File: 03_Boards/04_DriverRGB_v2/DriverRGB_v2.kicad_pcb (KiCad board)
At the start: 2 copper layers, 30 x 45 mm, 22 parts, among them J1 PJ-102A, J2 S4B-ZR-SM4A, J3 AMPHENOL_20021121-00006C1LF, Q1 DPAK3-CASE-369AS, Q2 DPAK3-CASE-369AS, Q3 DPAK3-CASE-369AS, U1 MODULE_ESP-12S, U3 AMS1117CD-3.3

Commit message: Docimentation
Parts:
- moved J1 1.68 mm to (142.3, 85.0)
- moved C3 1.31 mm to (140.8, 81.9)
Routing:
- net GND: track 55.1 -> 56.8 mm
- net PWR_IN: track 65.7 -> 66.8 mm
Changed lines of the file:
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@@
     (pad_to_mask_clearance 0)
     (pcbplotparams
-      (layerselection 0x003ffff_ffffffff)
+      (layerselection 0x003f0ff_ffffffff)
       (plot_on_all_layers_selection 0x0000000_00000000)
       (disableapertmacros false)
@@
       (dashed_line_gap_ratio 3.000000)
       (svgprecision 4)
-      (plotframeref false)
+      (plotframeref true)
       (viasonmask false)
       (mode 1)
@@
   )
   (footprint "01_Footprints:PJ-102AH" (layer "F.Cu")
-    (at 142.367 86.6394)
+    (at 142.3162 84.963)
     (descr "PJ-102AH")
     (tags "Connector")
@@
     (property "ki_keywords" "CP-102A-ND")
     (attr through_hole)
-    (fp_text reference "J1" (at -1.905 -8.89) (layer "F.SilkS")
+    (fp_text reference "J1" (at -1.9304 -7.8994) (layer "F.SilkS")
         (effects (font (size 1.27 1.27) (thickness 0.254) bold))
     )
@@
         (effects (font (size 1.27 1.27) (thickness 0.254)))
     )
-    (fp_line (start 0 -10.7) (end 0 -3.5)
+    (fp_line (start 0 -9.144) (end 0 -3.5)
       (stroke (width 0.2) (type solid)) (layer "F.SilkS"))
-    (fp_line (start 9 -10.7) (end 0 -10.7)
+    (fp_line (start 9 -9.144) (end 0 -9.144)
       (stroke (width 0.2) (type solid)) (layer "F.SilkS"))
-    (fp_line (start 9 3.7) (end 9 -10.7)
+    (fp_line (start 9 3.7) (end 9 -9.144)
       (stroke (width 0.2) (type solid)) (layer "F.SilkS"))
     (fp_circle (center 4.261 5.051) (end 4.261 5.16985)
@@
   )
   (footprint "Capacitor_SMD:C_0603_1608Metric" (layer "B.Cu")
-    (at 140.843 83.1974 90)
+    (at 140.843 81.8896 90)
     (descr "Capacitor SMD 0603 (1608 Metric), square (rectangular) end terminal, IPC_7351 nominal, (Body size source: IPC-SM-782 page 76, https://www.pcb-3d.com/wordpress/wp-content/uploads/ipc-sm-782a_amendment_1_and_2.pdf), generated with kicad-footprint-generator")
     (tags "capacitor")
@@
     (property "ki_keywords" "cap capacitor")
     (attr smd)
-    (fp_text reference "C3" (at -0.013 1.778 180) (layer "B.SilkS")
+    (fp_text reference "C3" (at 1.143 -1.8034 180) (layer "B.SilkS")
         (effects (font (size 1 1) (thickness 0.2) bold) (justify mirror))
     )
@@
   (segment (start 142.748 116.4354) (end 143.764 115.4194) (width 0.3) (layer "B.Cu") (net 1))
   (segment (start 147.3454 101.6762) (end 148.336 102.6668) (width 0.7) (layer "F.Cu") (net 2))
-  (segment (start 140.1378 100.36545) (end 140.1378 88.4686) (width 0.7) (layer "F.Cu") (net 2))
   (segment (start 146.3548 102.6414) (end 147.326 101.6702) (width 0.7) (layer "F.Cu") (net 2))
+  (segment (start 140.1378 86.7414) (end 141.9162 84.963) (width 0.7) (layer "F.Cu") (net 2))
   (segment (start 141.1478 102.6414) (end 146.3548 102.6414) (width 0.7) (layer "F.Cu") (net 2))
   (segment (start 140.1378 100.36545) (end 140.1378 101.6314) (width 0.7) (layer "F.Cu") (net 2))
@@
   (segment (start 147.3454 100.3808) (end 147.3454 101.6762) (width 0.7) (layer "F.Cu") (net 2))
   (segment (start 147.326 101.6702) (end 147.326 100.3816) (width 0.7) (layer "F.Cu") (net 2))
-  (segment (start 140.1378 88.4686) (end 141.967 86.6394) (width 0.7) (layer "F.Cu") (net 2))
+  (segment (start 140.1378 100.36545) (end 140.1378 86.7414) (width 0.7) (layer "F.Cu") (net 2))
   (segment (start 140.1378 101.6314) (end 141.1478 102.6414) (width 0.7) (layer "F.Cu") (net 2))
   (segment (start 153.6192 102.6668) (end 154.6218 101.6642) (width 0.7) (layer "F.Cu") (net 2))
@@
   (segment (start 154.051 118.1354) (end 151.498 118.1354) (width 0.3) (layer "B.Cu") (net 3))
   (segment (start 138.557 80.9244) (end 138.557 83.0304) (width 0.3) (layer "B.Cu") (net 4))
+  (segment (start 138.9228 82.6646) (end 138.557 83.0304) (width 0.3) (layer "B.Cu") (net 4))
   (segment (start 153.914 82.9244) (end 153.914 82.4384) (width 0.3) (layer "B.Cu") (net 4))
-  (segment (start 138.885 83.0304) (end 138.557 83.0304) (width 0.3) (layer "B.Cu") (net 4))
-  (segment (start 140.843 83.9724) (end 139.827 83.9724) (width 0.3) (layer "B.Cu") (net 4))
+  (segment (start 140.843 82.6646) (end 138.9228 82.6646) (width 0.3) (layer "B.Cu") (net 4))
   (segment (start 153.914 82.4384) (end 151.257 79.7814) (width 0.3) (layer "B.Cu") (net 4))
-  (segment (start 139.827 83.9724) (end 138.885 83.0304) (width 0.3) (layer "B.Cu") (net 4))
   (segment (start 151.257 79.7814) (end 139.7 79.7814) (width 0.3) (layer "B.Cu") (net 4))
   (segment (start 139.7 79.7814) (end 138.557 80.9244) (width 0.3) (layer "B.Cu") (net 4))
@@
   (segment (start 154.5696 95.032) (end 151.638 92.1004) (width 0.3) (layer "B.Cu") (net 5))
   (segment (start 154.5696 96.5446) (end 154.5696 95.1776) (width 0.3) (layer "B.Cu") (net 5))
+  (segment (start 144.7398 116.3128) (end 145.3686 116.9416) (width 0.7) (layer "F.Cu") (net 6))
+  (segment (start 152.7076 87.963) (end 146.6162 87.963) (width 0.7) (layer "F.Cu") (net 6))
+  (segment (start 154.686 116.9416) (end 160.9598 110.6678) (width 0.7) (layer "F.Cu") (net 6))
+  (segment (start 144.7398 115.0112) (end 144.7398 116.3128) (width 0.7) (layer "F.Cu") (net 6))
+  (segment (start 160.9598 96.2152) (end 152.7076 87.963) (width 0.7) (layer "F.Cu") (net 6))
   (segment (start 160.9598 110.6678) (end 160.9598 96.2152) (width 0.7) (layer "F.Cu") (net 6))
-  (segment (start 144.7398 116.3128) (end 145.3686 116.9416) (width 0.7) (layer "F.Cu") (net 6))
-  (segment (start 144.7398 115.0112) (end 144.7398 116.3128) (width 0.7) (layer "F.Cu") (net 6))
-  (segment (start 160.9598 96.2152) (end 154.384 89.6394) (width 0.7) (layer "F.Cu") (net 6))
   (segment (start 145.3686 116.9416) (end 154.686 116.9416) (width 0.7) (layer "F.Cu") (net 6))
-  (segment (start 154.686 116.9416) (end 160.9598 110.6678) (width 0.7) (layer "F.Cu") (net 6))
-  (segment (start 146.842 89.4644) (end 146.667 89.6394) (width 0.7) (layer "F.Cu") (net 6))
-  (segment (start 154.384 89.6394) (end 146.667 89.6394) (width 0.7) (layer "F.Cu") (net 6))
-  (segment (start 157.373 89.4644) (end 146.842 89.4644) (width 0.3) (layer "B.Cu") (net 6))
-  (segment (start 159.014 91.1054) (end 157.373 89.4644) (width 0.3) (layer "B.Cu") (net 6))
+  (segment (start 155.8716 87.963) (end 146.6162 87.963) (width 0.3) (layer "B.Cu") (net 6))
   (segment (start 159.014 91.6244) (end 159.014 91.1054) (width 0.3) (layer "B.Cu") (net 6))
-  (segment (start 146.842 89.4644) (end 146.667 89.6394) (width 0.3) (layer "B.Cu") (net 6))
+  (segment (start 159.014 91.1054) (end 155.8716 87.963) (width 0.3) (layer "B.Cu") (net 6))
   (segment (start 149.2398 114.4428) (end 156.9018 106.7808) (width 0.7) (layer "F.Cu") (net 7))
   (segment (start 149.2398 115.0112) (end 149.2398 114.4428) (width 0.7) (layer "F.Cu") (net 7))

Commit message: PCB
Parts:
- added R8: 10kOhm, Resistor_SMD:R_0603_1608Metric, B.Cu at (151.2, 117.2)
- C1, C2: value 100nF -> 1nF
- J3: value AMPHENOL_20021121-00006C1LF -> 20021121-00006C1LF
- Q1, Q2, Q3: value DPAK3-CASE-369AS -> FDD8880
- S1: value Enable -> Reset
- S2: value IO0 -> Boot
- U1: value MODULE_ESP-12S -> ESP-12S
- moved C3 6.39 mm to (141.0, 88.3), turned to -90 degrees
- moved C2 4.67 mm to (156.1, 117.3)
- moved S2 0.43 mm to (153.6, 116.4)
- moved R7 0.13 mm to (142.6, 117.3)
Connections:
- R7 pad 1: EN -> VDD
- R7 pad 2: GND -> EN
- S1 pad 1: EN -> GND
- S1 pad 2: VDD -> EN
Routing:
- net GND: track 56.8 -> 71.3 mm
- net EN: track 29.9 -> 35.2 mm
- net IO0: track 12.0 -> 16.4 mm
- net Net-(D1-+): track 22.0 -> 25.0 mm
- net VDD: track 54.3 -> 55.6 mm
- net PWR_IN: track 66.8 -> 68.0 mm

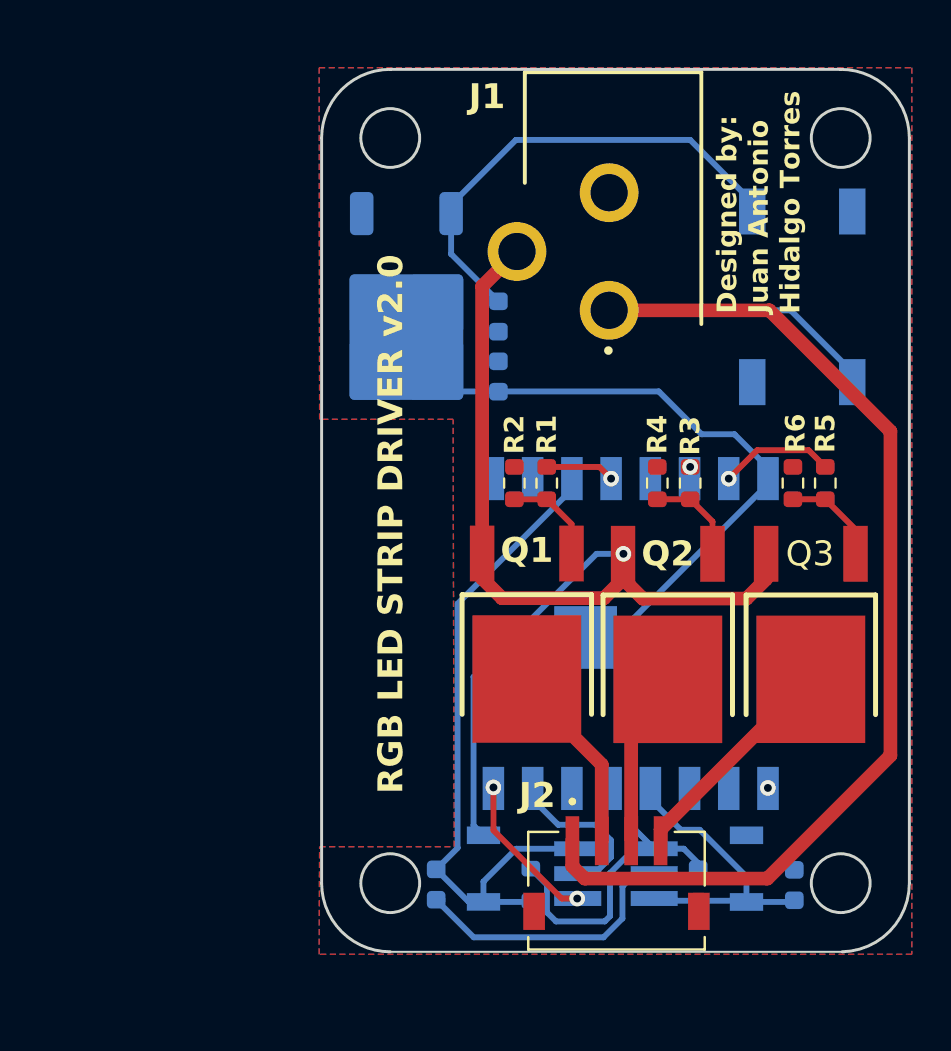
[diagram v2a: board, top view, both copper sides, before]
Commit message: Rediseño del esquemático del PCB
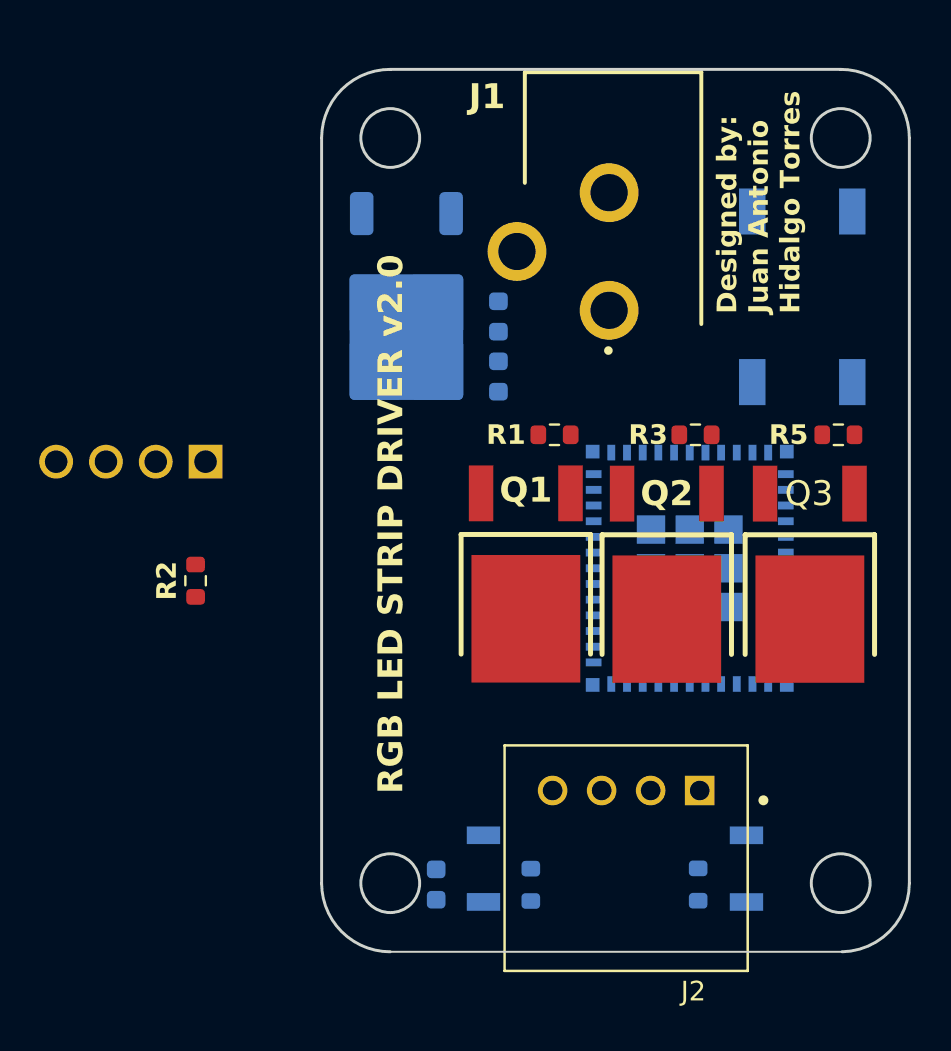
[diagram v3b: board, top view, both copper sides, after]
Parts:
- removed C2: 1nF, Capacitor_SMD:C_0603_1608Metric
- removed R4, R6: 10kOhm, Resistor_SMD:R_0603_1608Metric
- removed U1: ESP-12S, 01_Footprints:ESP-12S
- added IC1: ESP32C6MINI1N4, 01_Footprints:ESP32-C6-MINI-1-N4, B.Cu at (150.7, 101.1)
- C1: value 1nF -> 100nF
- J2: value S4B-ZR-SM4A -> S4B-XH-A_LF__SN_; footprint 01_Footprints:S4B-ZR-SM4A-TF-LF -> 01_Footprints:S4B-XH-A_LF__SN_
- J3: value 20021121-00006C1LF -> 61300411121; footprint 01_Footprints:20021121-00006C1LF -> 01_Footprints:61300411121
- moved J3 29.7 mm to (126.0, 95.7), turned to 180 degrees
- moved R2 17.0 mm to (125.5, 101.8)
- moved Q1 3.07 mm to (142.4, 103.7)
- moved Q3 3.07 mm to (156.9, 103.7)
- moved Q2 3.07 mm to (149.6, 103.7)
- moved J2 2.61 mm to (147.5, 112.5), turned to 180 degrees
- moved R5 2.55 mm to (158.3, 94.3), turned to 0 degrees
- moved R1 2.50 mm to (143.8, 94.3), turned to 0 degrees
- moved R3 2.48 mm to (151.0, 94.3), turned to 0 degrees
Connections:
- J3 pad 1: EN -> GND
- J3 pad 2: VDD -> TX
- J3 pad 3: TX -> RX
- J3 pad 4: GND -> VDD
- R2 pad 1: GND -> VDD
- R2 pad 2: Net-(Q1-G) -> Net-(IC1-IO8)
- R8 pad 2: IO0 -> IO9
- S2 pad 2: IO0 -> IO9
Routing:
- net GND: track 71.3 -> 0.00 mm, vias 2 -> 0
- net PWR_IN: track 68.0 -> 0.00 mm
- net VDD: track 55.6 -> 0.00 mm
- net EN: track 35.2 -> 0.00 mm
- net Net-(D1-+): track 25.0 -> 0.00 mm
- net IO0: track 16.4 -> 0.00 mm
- net BLUE_OUT-: track 11.4 -> 0.00 mm
- net RED_OUT-: track 9.83 -> 0.00 mm
- net GREEN_OUT-: track 9.00 -> 0.00 mm
- net RX: track 8.97 -> 0.00 mm, vias 2 -> 0
- net TX: track 8.32 -> 0.00 mm
- net PWM_BLUE: track 5.87 -> 0.00 mm, vias 1 -> 0
- net Net-(Q3-G): track 5.07 -> 0.00 mm
- net Net-(Q1-G): track 4.94 -> 0.00 mm
- net PWM_RED: track 3.53 -> 0.00 mm, vias 1 -> 0
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- removed copper zone on B.Cu, net GND
- removed copper zone on F.Cu, net GND

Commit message: Board desing v2
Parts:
- IC1: value ESP32C6MINI1N4 -> ESP32-C6-MINI-1-N4
- R2: moved to B.Cu
- moved S2 22.9 mm to (139.8, 98.2)
- moved R6 21.1 mm to (142.2, 98.2)
- moved R4 18.6 mm to (139.8, 94.4)
- moved Q3 18.5 mm to (138.4, 103.7)
- moved R2 16.7 mm to (142.2, 102.4), turned to 90 degrees
- moved R5 15.9 mm to (139.7, 101.6), turned to 0 degrees
- moved C1 14.0 mm to (139.7, 103.4), turned to 180 degrees
- moved Q1 10.2 mm to (152.6, 103.7)
- moved R1 10.1 mm to (153.9, 94.4)
- moved S1 9.72 mm to (139.8, 106.7), turned to 90 degrees
- moved J3 8.24 mm to (133.7, 98.7), turned to -90 degrees
- moved R3 4.15 mm to (146.9, 94.4)
- moved Q2 4.13 mm to (145.4, 103.7)
- moved IC1 1.36 mm to (150.7, 102.5)
- moved D1 0.64 mm to (156.4, 86.6), turned to 90 degrees
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- renumbered C3 to C2, C4 to C3, R5 to R4, R7 to R5, R8 to R6, U3 to U1
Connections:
- IC1 pad 26: PWM_RED -> PWM_BLUE
- IC1 pad 27: PWM_BLUE -> PWM_GREEN
- IC1 pad 28: PWM_GREEN -> PWM_RED
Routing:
- net VDD: track 0.00 -> 71.3 mm, vias 0 -> 1
- net GND: track 0.00 -> 55.6 mm, vias 0 -> 2
- net PWR_IN: track 0.00 -> 36.0 mm
- net RX: track 0.00 -> 33.7 mm
- net TX: track 0.00 -> 32.2 mm
- net Net-(D1-+): track 0.00 -> 26.6 mm
- net EN: track 0.00 -> 16.3 mm
- net RED_OUT-: track 0.00 -> 15.5 mm
- net BLUE_OUT-: track 0.00 -> 11.0 mm
- net PWM_BLUE: track 0.00 -> 9.93 mm, vias 0 -> 1
- net GREEN_OUT-: track 0.00 -> 9.12 mm
- net IO9: track 0.00 -> 6.61 mm
- net PWM_RED: track 0.00 -> 5.56 mm, vias 0 -> 1
- net Net-(IC1-IO8): track 0.00 -> 4.51 mm
- net PWM_GREEN: track 0.00 -> 3.80 mm, vias 0 -> 1
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- added copper zone on B.Cu, net GND
- added copper zone on F.Cu, net GND

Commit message: Documentation
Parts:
- added REF**: OSHW-Logo2_9.8x8mm_SilkScreen, Symbol:OSHW-Logo2_9.8x8mm_SilkScreen, F.Cu at (157.0, 85.0)
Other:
- board text removed: "Designed by: Juan Antonio Hidalgo Torres"
- board text removed: "RGB LED STRIP DRIVER v2.0"
